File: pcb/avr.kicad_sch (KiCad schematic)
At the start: 17 parts, among them J11 PEN, J14 ATMegaSpare, J16 ATUART, J18 Reset ext, J4 AVR ISP, J6 Enable load, SW2 Reset btn, U22 ATmega128L-8A, Y3 16MHz

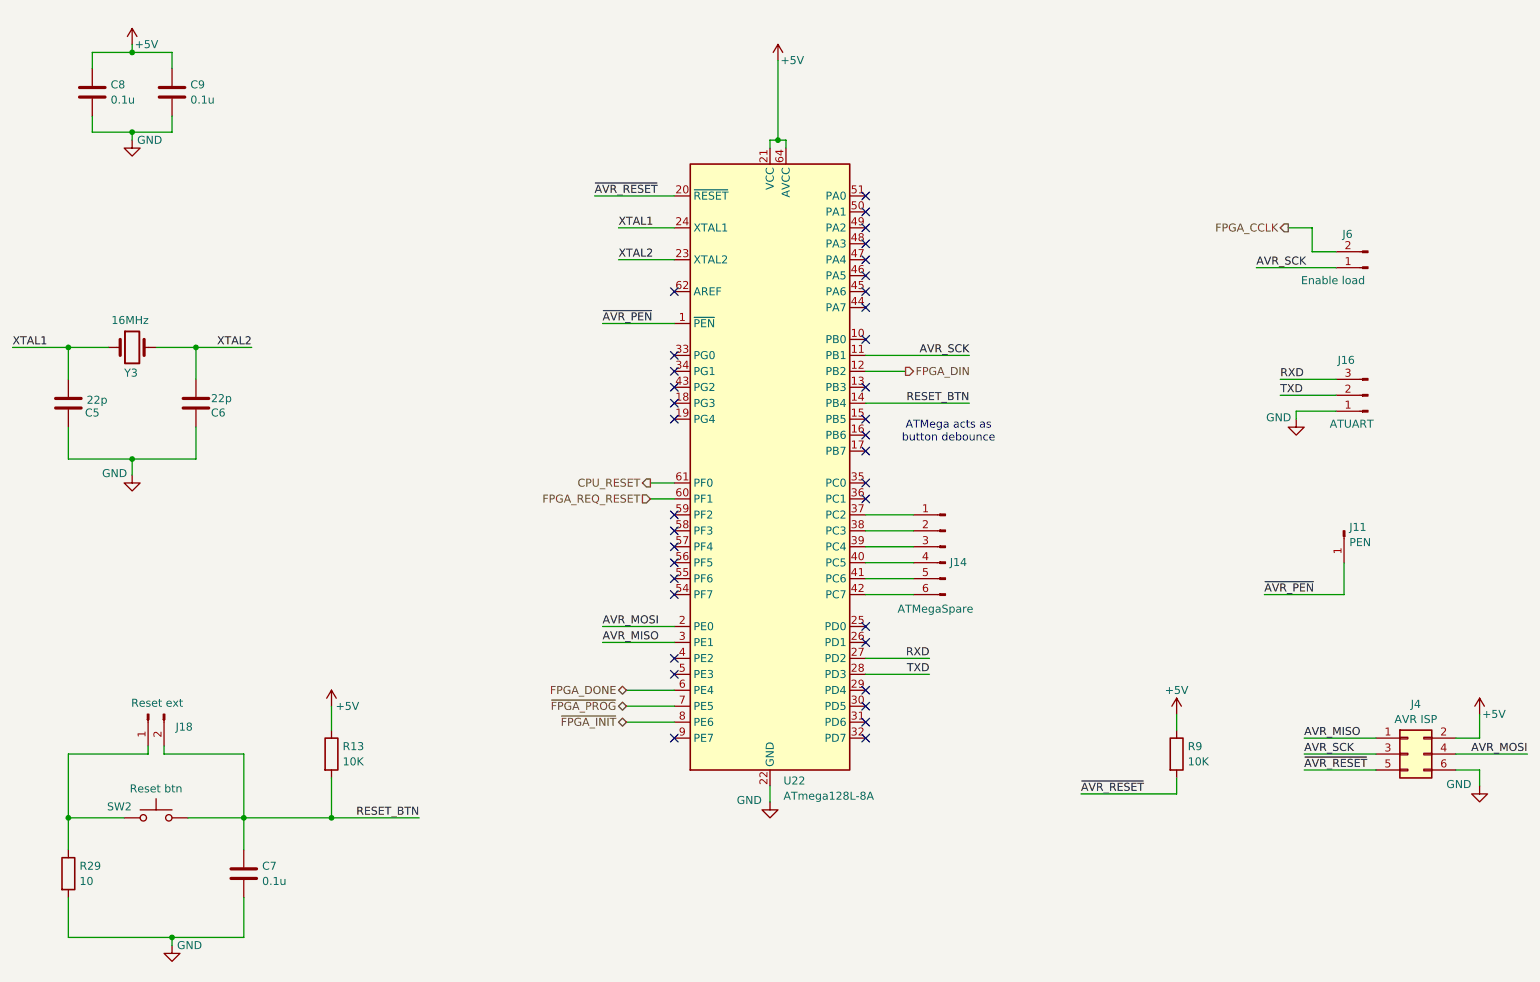
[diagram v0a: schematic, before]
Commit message: avr bus_tr diagrams aligned to grid
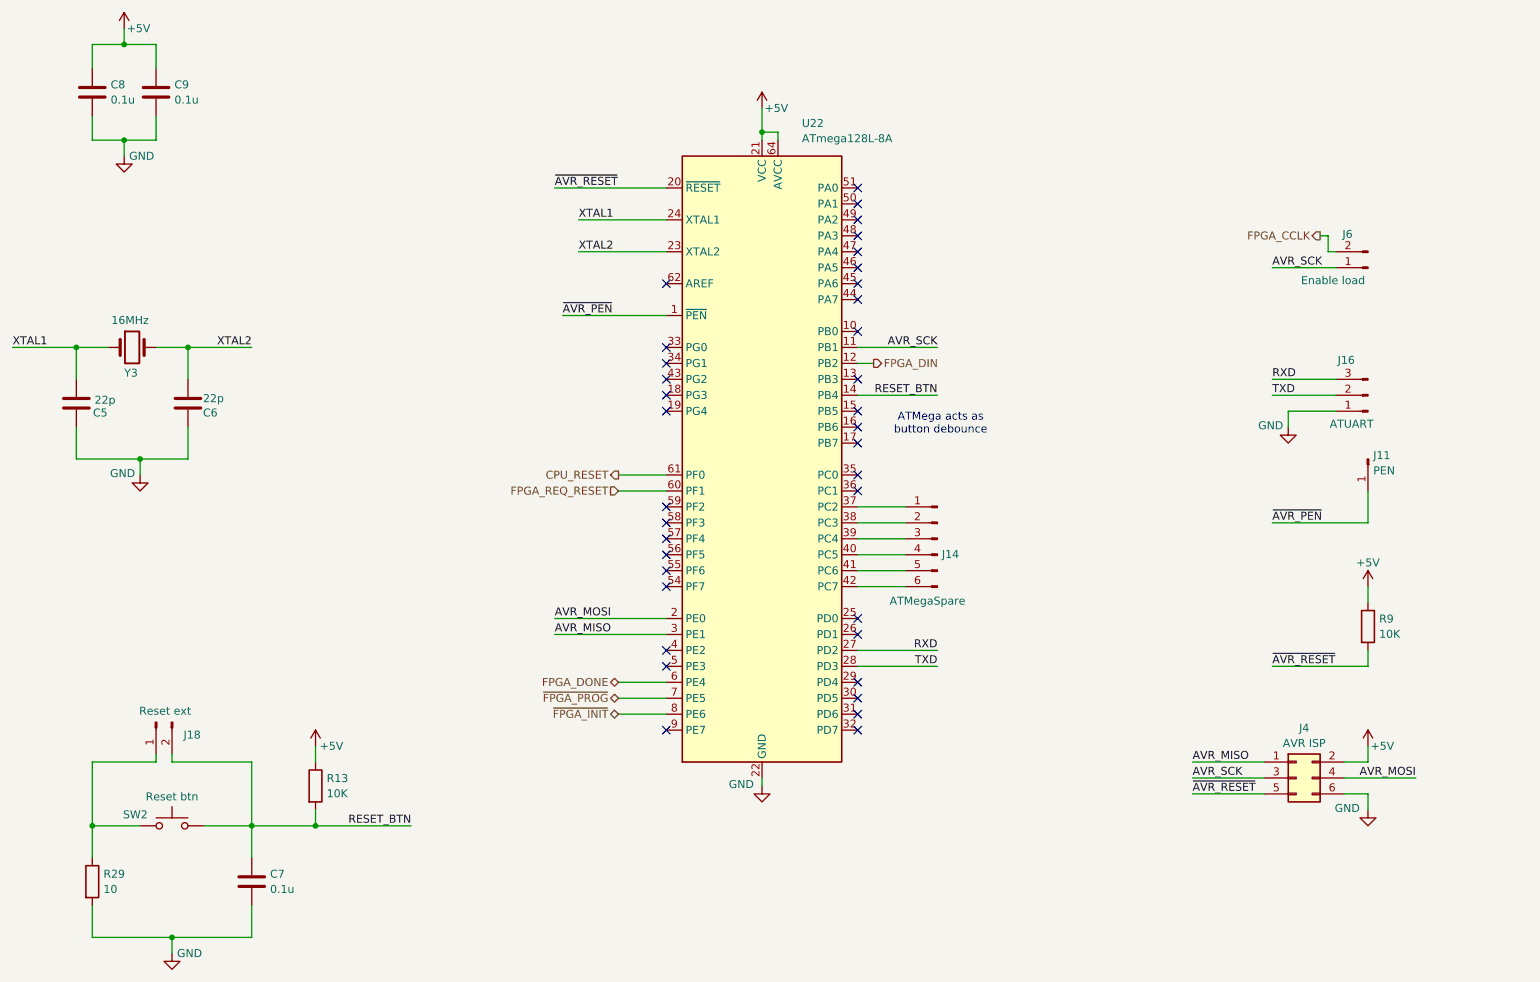
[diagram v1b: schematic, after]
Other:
- moved on the sheet: C5, C6, C7, C9, J11, J14, J18, J4, R13, R29, R9, SW2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
